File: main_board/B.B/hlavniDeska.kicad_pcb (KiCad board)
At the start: 4 copper layers, 98 x 98 mm, 118 parts, among them J1 Conn_01x04, J2 Conn_01x11, J4 Conn_01x04, J5 USB_C_Receptacle_USB2.0, M1 Motor_DC, Q1 2N7002, Q10 2N7002, Q11 SI3447CDV, Q2 2N7002, Q3 AO3400A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

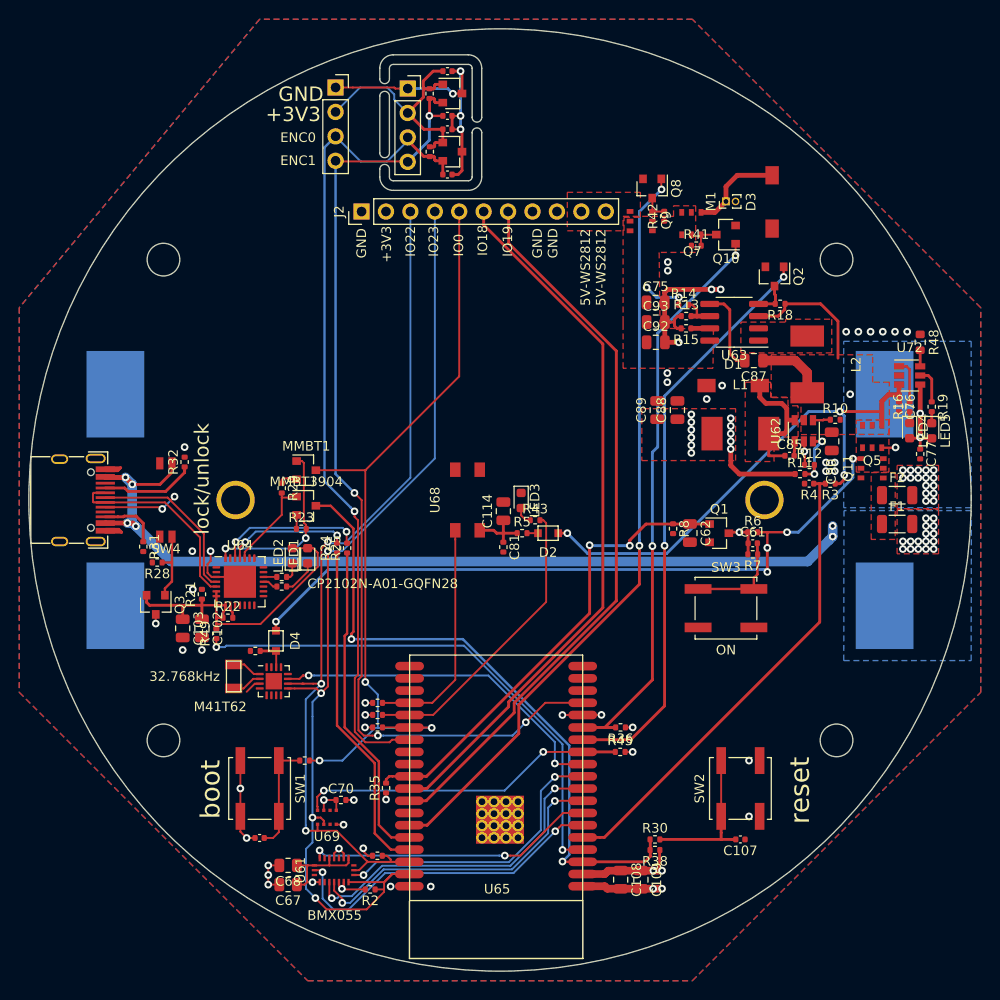
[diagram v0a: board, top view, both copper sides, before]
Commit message: JLCdata
- korekce pozice a natoceni
- data pro vyrobu
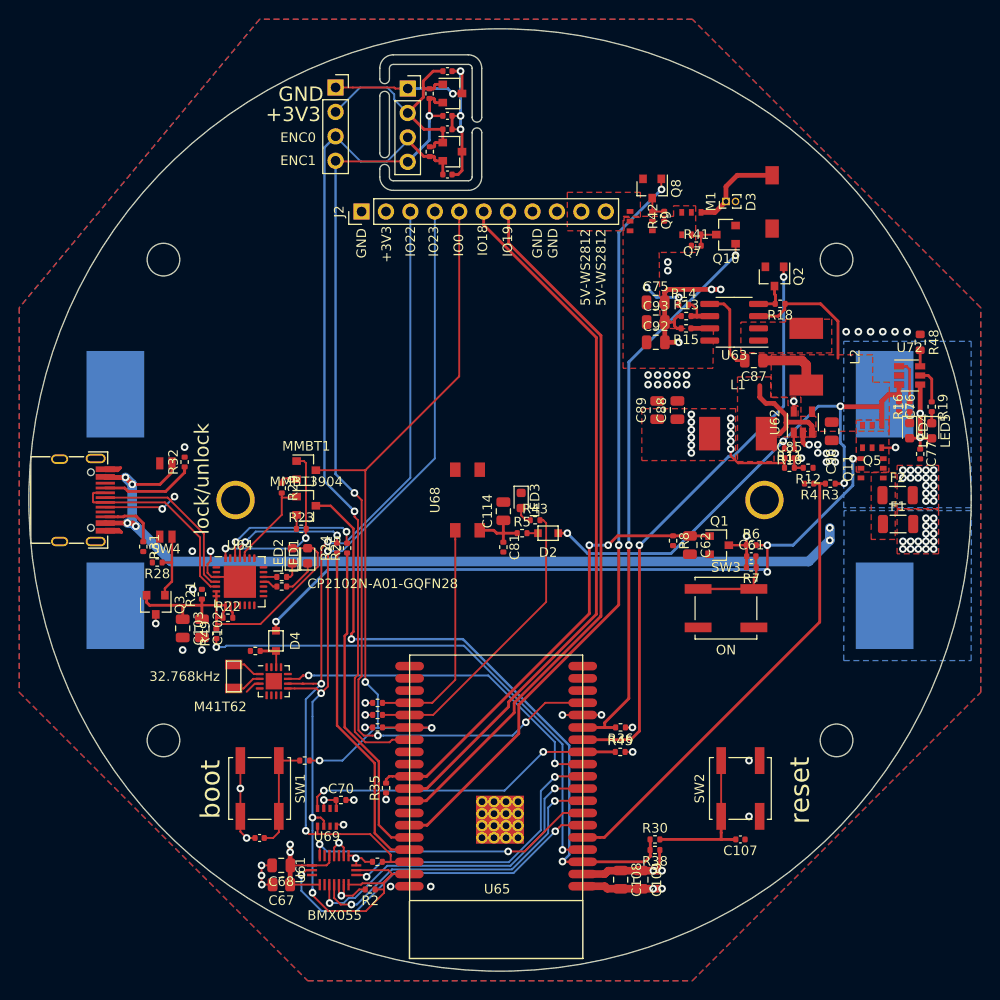
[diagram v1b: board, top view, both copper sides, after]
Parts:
- removed D1: SS54, BB:DO-214AC
- C68: footprint Resistor_SMD:R_0805_2012Metric -> Capacitor_SMD:C_0805_2012Metric
- C85: value 10nf -> 22nf
- U62: value AOZ1280 -> SY8009; footprint Package_TO_SOT_SMD:SOT-23-6 -> Package_TO_SOT_SMD:SOT-23-5
- moved R10 5.63 mm to (230.1, 94.7), turned to 180 degrees
- moved R6 1.36 mm to (226.1, 104.7)
- moved C61 1.36 mm to (226.1, 105.8)
- moved R7 1.36 mm to (226.1, 107.0)
- moved R11 1.28 mm to (230.1, 96.7)
- moved C62 1.25 mm to (219.8, 104.7)
- moved Q1 1.25 mm to (222.8, 104.7)
- moved R8 1.25 mm to (218.0, 104.2)
- moved C90 1.05 mm to (234.5, 92.8)
- moved U62 0.91 mm to (231.5, 91.9)
- moved L2 0.81 mm to (231.8, 85.1)
- moved C68 0.71 mm to (177.2, 138.0)
- moved C67 0.70 mm to (177.3, 140.0)
- moved R1 0.63 mm to (187.2, 137.6)
- moved R12 0.33 mm to (232.1, 96.7), turned to 180 degrees
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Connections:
- C85 pad 1: Net-(C85-Pad1) -> +3V3
- L1 pad 1: Net-(C85-Pad1) -> Net-(L1-Pad1)
- R11 pad 2: Net-(R11-Pad2) -> Net-(C85-Pad2)
- R12 pad 2: Net-(R11-Pad2) -> Net-(C85-Pad2)
- U62 pad 1: Net-(C85-Pad2) -> Net-(R10-Pad1)
- U62 pad 3: Net-(R11-Pad2) -> Net-(L1-Pad1)
- U62 pad 4: Net-(R10-Pad1) -> VCC
- U62 pad 5: VCC -> Net-(C85-Pad2)
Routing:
- net Net-(C85-Pad1): track 13.5 -> 0.00 mm
- net Net-(L1-Pad1): track 0.00 -> 11.9 mm
- net Net-(C85-Pad2): track 1.52 -> 9.78 mm, vias 0 -> 2
- net Net-(R11-Pad2): track 6.68 -> 0.00 mm, vias 2 -> 0
- net +3V3: track 69.3 -> 73.2 mm, vias 21 -> 22
- net /ESP3200/IO23: track 101.8 -> 105.5 mm
- net /ESP3200/IO34: track 34.8 -> 36.8 mm
- net VCC: track 76.4 -> 78.1 mm
- net /ESP3200/IO22: track 89.7 -> 88.1 mm
- net Net-(C61-Pad2): track 10.7 -> 9.33 mm
- net /ESP3200/IO19: track 75.9 -> 74.6 mm
- net /ESP3200/IO33: track 34.6 -> 35.5 mm
- net /ESP3200/IO5-up: track 49.6 -> 48.7 mm
- net /ESP3200/IO18: track 74.6 -> 74.0 mm
- net /ESP3200/IO35: track 30.2 -> 30.8 mm
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- added copper zone on F.Cu, net Net-(L1-Pad1)
- removed copper zone on F.Cu, net Net-(C85-Pad1)
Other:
- rule via_min_size: 0.4 -> 0.35
